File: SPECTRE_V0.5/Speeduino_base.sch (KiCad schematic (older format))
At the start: 209 parts, among them J1 Conn_01x04_Male, J2 Conn_02x04_Odd_Even, J3 Conn_01x06_Male, Q1 2N7002, Q10 BSP78, Q11 BSP78, Q12 BSP78, Q13 BSP78, Q14 BSP78, Q15 BSP78, Q16 SMD-MOSFET-N-CH-30V-5.8A-AO34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, Q17 AO3401A, Q18 BSP78, Q19 SMD-MOSFET-N-CH-30V-5.8A-AO34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, Q2 CJ2302, Q20 AO3401A, Q21 SMD-MOSFET-N-CH-30V-5.8A-AO34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, Q22 SMD-MOSFET-N-CH-30V-5.8A-AO34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, Q23 AO3401A, Q24 AO3401A, Q25 BSP78, Q26 BSP78, Q3 CJ2302, Q4 CJ2302, Q5 BSP78, Q6 BSP78, Q7 CJ2302, Q8 CJ2302, Q9 CJ2302, U1 MAX9926UAEE+, U2 molex_48pin, U3 LM78M05_TO220, U4 MAX3232

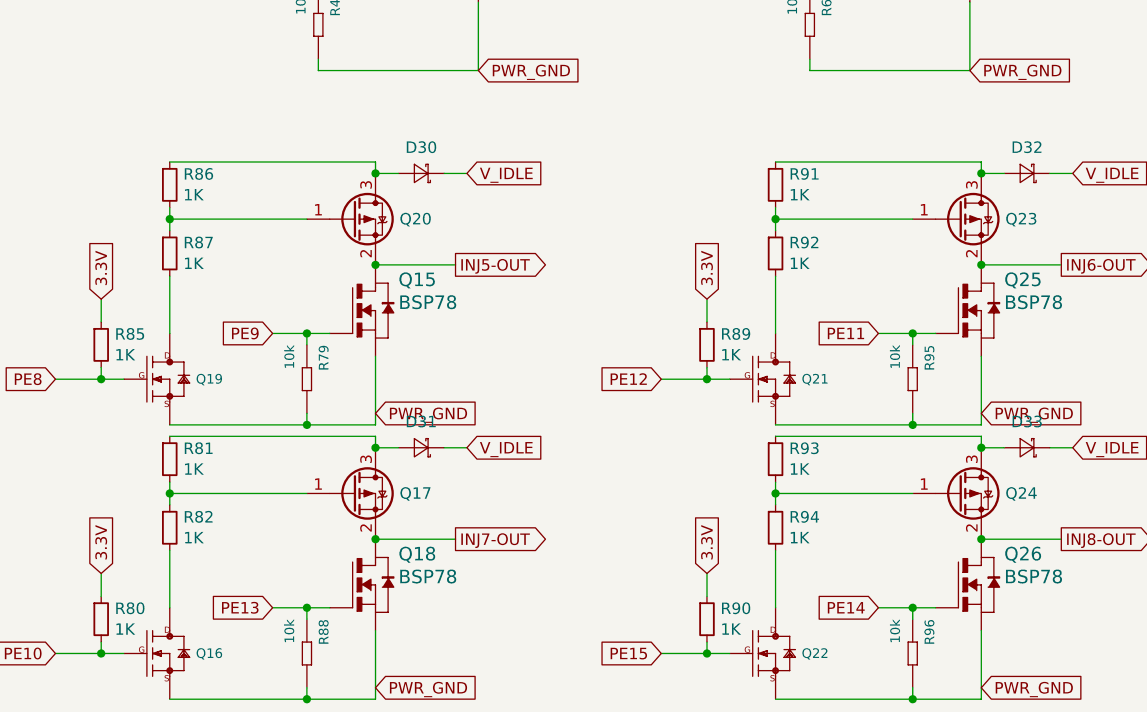
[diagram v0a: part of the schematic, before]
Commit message: peak & hold injector driver update
Updates to Low-z PWM peak & hold injector driver schematic.
Updates simulation low-z driver.
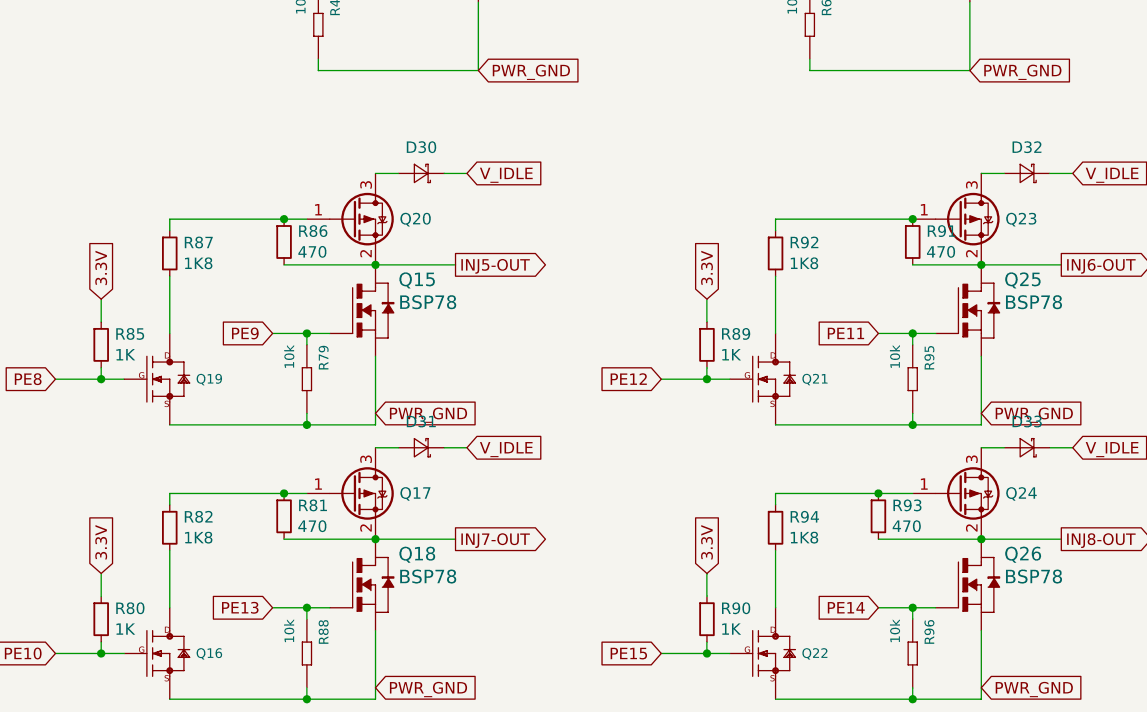
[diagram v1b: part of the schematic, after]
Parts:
- Q16, Q19, Q21, Q22: value SMD-MOSFET-N-CH-30V-5.8A-AO3400(SOT-23) -> SMD-MOSFET-N-CH-55V-2.1A-AO3422(SOT-23)
- R81, R86, R91, R93: value 1K -> 470
- R82, R87, R92, R94: value 1K -> 1K8
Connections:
- wire segments 554 -> 549
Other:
- moved on the sheet: R81, R86, R91, R93
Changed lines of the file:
@@
 P 12550 10250
 F 0 "Q19" H 12664 10250 42  0000 L CNN
-F 1 "SMD-MOSFET-N-CH-30V-5.8A-AO3400(SOT-23)" H 12664 10211 42  0001 L CNN
+F 1 "SMD-MOSFET-N-CH-55V-2.1A-AO3422(SOT-23)" H 12664 10211 42  0001 L CNN
 F 2 "Package_TO_SOT_SMD:SOT-23_Handsoldering" H 12550 10250 50  0001 C CNN
 F 3 "" H 12550 10250 50  0001 C CNN
@@
 L Device:R_Small R86
 U 1 1 5EAAD26C
-P 12550 9400
-F 0 "R86" H 12609 9446 50  0000 L CNN
-F 1 "1K" H 12609 9355 50  0000 L CNN
-F 2 "Speeduino_base:R_0603_1608Metric_Pad1.05x0.95mm_HandSolder" H 12550 9400 50  0001 C CNN
-F 3 "~" H 12550 9400 50  0001 C CNN
-	1    12550 9400
+P 13050 9650
+F 0 "R86" H 13109 9696 50  0000 L CNN
+F 1 "470" H 13109 9605 50  0000 L CNN
+F 2 "Speeduino_base:R_0603_1608Metric_Pad1.05x0.95mm_HandSolder" H 13050 9650 50  0001 C CNN
+F 3 "~" H 13050 9650 50  0001 C CNN
+	1    13050 9650
 	1    0    0    -1
 $EndComp
@@
 P 12550 9700
 F 0 "R87" H 12609 9746 50  0000 L CNN
-F 1 "1K" H 12609 9655 50  0000 L CNN
+F 1 "1K8" H 12609 9655 50  0000 L CNN
 F 2 "Speeduino_base:R_0603_1608Metric_Pad1.05x0.95mm_HandSolder" H 12550 9700 50  0001 C CNN
 F 3 "~" H 12550 9700 50  0001 C CNN
@@
 	12550 9600 12550 9550
 Wire Wire Line
-	12550 9550 13150 9550
-Connection ~ 12550 9550
-Wire Wire Line
-	12550 9550 12550 9500
+	12550 9550 13050 9550
 $Comp
 L Device:R_Small R85
@@
 P 12550 11450
 F 0 "Q16" H 12664 11450 42  0000 L CNN
-F 1 "SMD-MOSFET-N-CH-30V-5.8A-AO3400(SOT-23)" H 12664 11411 42  0001 L CNN
+F 1 "SMD-MOSFET-N-CH-55V-2.1A-AO3422(SOT-23)" H 12664 11411 42  0001 L CNN
 F 2 "Package_TO_SOT_SMD:SOT-23_Handsoldering" H 12550 11450 50  0001 C CNN
 F 3 "" H 12550 11450 50  0001 C CNN
@@
 L Device:R_Small R81
 U 1 1 5F250B2A
-P 12550 10600
-F 0 "R81" H 12609 10646 50  0000 L CNN
-F 1 "1K" H 12609 10555 50  0000 L CNN
-F 2 "Speeduino_base:R_0603_1608Metric_Pad1.05x0.95mm_HandSolder" H 12550 10600 50  0001 C CNN
-F 3 "~" H 12550 10600 50  0001 C CNN
-	1    12550 10600
+P 13050 10850
+F 0 "R81" H 13109 10896 50  0000 L CNN
+F 1 "470" H 13109 10805 50  0000 L CNN
+F 2 "Speeduino_base:R_0603_1608Metric_Pad1.05x0.95mm_HandSolder" H 13050 10850 50  0001 C CNN
+F 3 "~" H 13050 10850 50  0001 C CNN
+	1    13050 10850
 	1    0    0    -1
 $EndComp
@@
 P 12550 10900
 F 0 "R82" H 12609 10946 50  0000 L CNN
-F 1 "1K" H 12609 10855 50  0000 L CNN
+F 1 "1K8" H 12609 10855 50  0000 L CNN
 F 2 "Speeduino_base:R_0603_1608Metric_Pad1.05x0.95mm_HandSolder" H 12550 10900 50  0001 C CNN
 F 3 "~" H 12550 10900 50  0001 C CNN
@@
 	13150 11250 13250 11250
 Connection ~ 13150 11250
-Wire Wire Line
-	13450 10950 13800 10950
 Wire Wire Line
 	13850 10550 13750 10550
@@
 	12550 10800 12550 10750
 Wire Wire Line
-	12550 10500 13450 10500
-Wire Wire Line
-	13450 10500 13450 10550
-Connection ~ 13450 10550
-Wire Wire Line
-	12550 10750 13150 10750
-Connection ~ 12550 10750
-Wire Wire Line
-	12550 10750 12550 10700
+	12550 10750 13050 10750
 $Comp
 L Device:R_Small R80
@@
 P 15200 10250
 F 0 "Q21" H 15314 10250 42  0000 L CNN
-F 1 "SMD-MOSFET-N-CH-30V-5.8A-AO3400(SOT-23)" H 15314 10211 42  0001 L CNN
+F 1 "SMD-MOSFET-N-CH-55V-2.1A-AO3422(SOT-23)" H 15314 10211 42  0001 L CNN
 F 2 "Package_TO_SOT_SMD:SOT-23_Handsoldering" H 15200 10250 50  0001 C CNN
 F 3 "" H 15200 10250 50  0001 C CNN
@@
 L Device:R_Small R91
 U 1 1 5F337FDE
-P 15200 9400
-F 0 "R91" H 15259 9446 50  0000 L CNN
-F 1 "1K" H 15259 9355 50  0000 L CNN
-F 2 "Speeduino_base:R_0603_1608Metric_Pad1.05x0.95mm_HandSolder" H 15200 9400 50  0001 C CNN
-F 3 "~" H 15200 9400 50  0001 C CNN
-	1    15200 9400
+P 15800 9650
+F 0 "R91" H 15859 9696 50  0000 L CNN
+F 1 "470" H 15859 9605 50  0000 L CNN
+F 2 "Speeduino_base:R_0603_1608Metric_Pad1.05x0.95mm_HandSolder" H 15800 9650 50  0001 C CNN
+F 3 "~" H 15800 9650 50  0001 C CNN
+	1    15800 9650
 	1    0    0    -1
 $EndComp
@@
 P 15200 9700
 F 0 "R92" H 15259 9746 50  0000 L CNN
-F 1 "1K" H 15259 9655 50  0000 L CNN
+F 1 "1K8" H 15259 9655 50  0000 L CNN
 F 2 "Speeduino_base:R_0603_1608Metric_Pad1.05x0.95mm_HandSolder" H 15200 9700 50  0001 C CNN
 F 3 "~" H 15200 9700 50  0001 C CNN
@@
 	15200 9600 15200 9550
 Wire Wire Line
-	15200 9300 16100 9300
-Wire Wire Line
-	16100 9300 16100 9350
-Connection ~ 16100 9350
-Wire Wire Line
 	15200 9550 15800 9550
-Connection ~ 15200 9550
-Wire Wire Line
-	15200 9550 15200 9500
 $Comp
 L Device:R_Small R89
@@
 P 15200 11450
 F 0 "Q22" H 15314 11450 42  0000 L CNN
-F 1 "SMD-MOSFET-N-CH-30V-5.8A-AO3400(SOT-23)" H 15314 11411 42  0001 L CNN
+F 1 "SMD-MOSFET-N-CH-55V-2.1A-AO3422(SOT-23)" H 15314 11411 42  0001 L CNN
 F 2 "Package_TO_SOT_SMD:SOT-23_Handsoldering" H 15200 11450 50  0001 C CNN
 F 3 "" H 15200 11450 50  0001 C CNN
@@
 L Device:R_Small R93
 U 1 1 5F33802C
-P 15200 10600
-F 0 "R93" H 15259 10646 50  0000 L CNN
-F 1 "1K" H 15259 10555 50  0000 L CNN
-F 2 "Speeduino_base:R_0603_1608Metric_Pad1.05x0.95mm_HandSolder" H 15200 10600 50  0001 C CNN
-F 3 "~" H 15200 10600 50  0001 C CNN
-	1    15200 10600
+P 15650 10850
+F 0 "R93" H 15709 10896 50  0000 L CNN
+F 1 "470" H 15709 10805 50  0000 L CNN
+F 2 "Speeduino_base:R_0603_1608Metric_Pad1.05x0.95mm_HandSolder" H 15650 10850 50  0001 C CNN
+F 3 "~" H 15650 10850 50  0001 C CNN
+	1    15650 10850
 	1    0    0    -1
 $EndComp
@@
 P 15200 10900
 F 0 "R94" H 15259 10946 50  0000 L CNN
-F 1 "1K" H 15259 10855 50  0000 L CNN
+F 1 "1K8" H 15259 10855 50  0000 L CNN
 F 2 "Speeduino_base:R_0603_1608Metric_Pad1.05x0.95mm_HandSolder" H 15200 10900 50  0001 C CNN
 F 3 "~" H 15200 10900 50  0001 C CNN
@@
 	15200 10800 15200 10750
 Wire Wire Line
-	15200 10500 16100 10500
-Wire Wire Line
-	16100 10500 16100 10550
-Connection ~ 16100 10550
-Wire Wire Line
-	15200 10750 15800 10750
-Connection ~ 15200 10750
-Wire Wire Line
-	15200 10750 15200 10700
+	15200 10750 15650 10750
 $Comp
 L Device:R_Small R90
@@
 Wire Wire Line
 	13450 9350 13550 9350
-Connection ~ 13450 9350
-Wire Wire Line
-	13450 9300 13450 9350
-Wire Wire Line
-	12550 9300 13450 9300
+Connection ~ 13050 9550
+Wire Wire Line
+	13050 9550 13150 9550
+Wire Wire Line
+	13050 9750 13450 9750
+Connection ~ 15800 9550
+Wire Wire Line
+	15800 9750 16100 9750
+Connection ~ 13050 10750
+Wire Wire Line
+	13050 10750 13150 10750
+Wire Wire Line
+	13050 10950 13450 10950
+Connection ~ 15650 10750
+Wire Wire Line
+	15650 10750 15800 10750
+Wire Wire Line
+	16100 10950 15650 10950
+Wire Wire Line
+	13450 10950 13800 10950
 $EndSCHEMATC

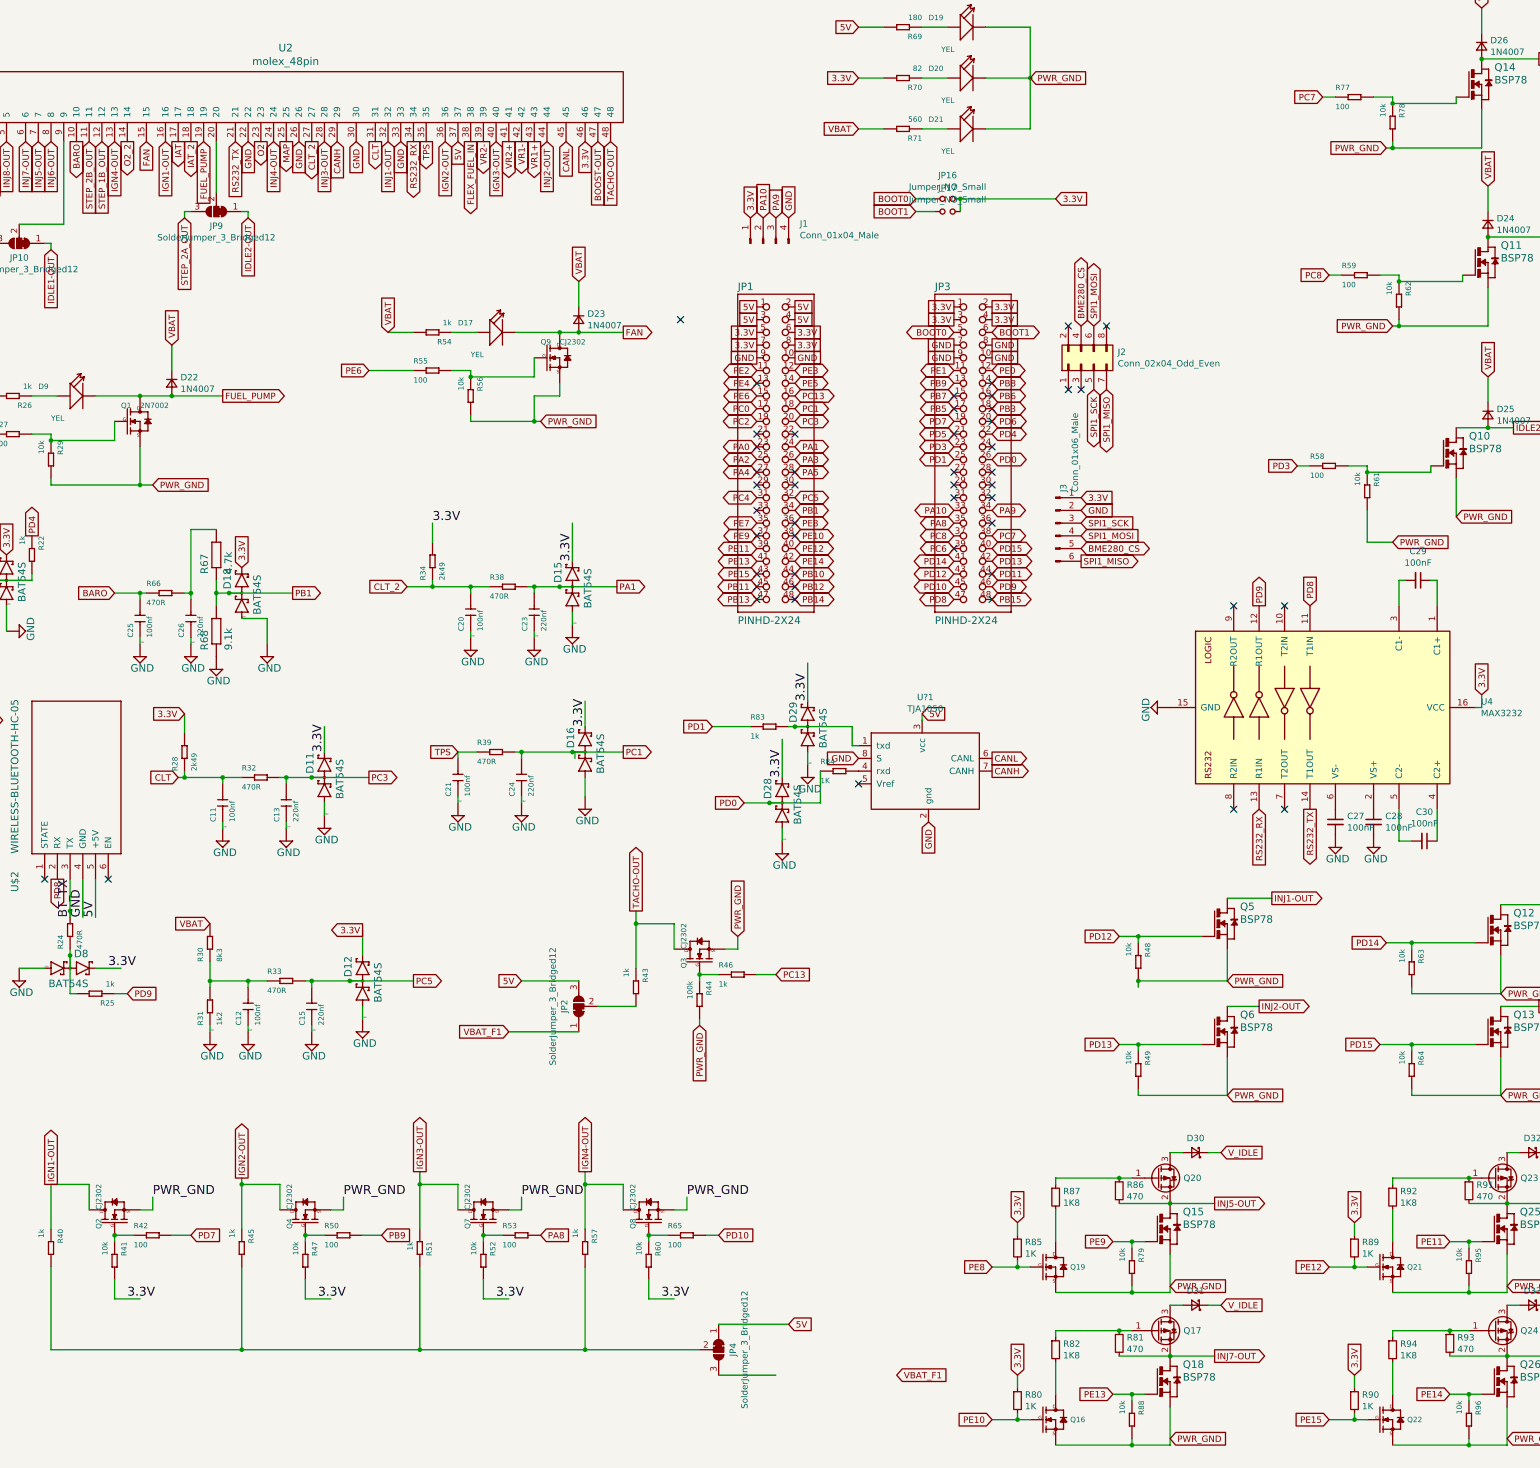
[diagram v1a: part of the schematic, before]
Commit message: Updates on routing V0.5 board
Switched some pins also updated the board routing a bit. not done yet.
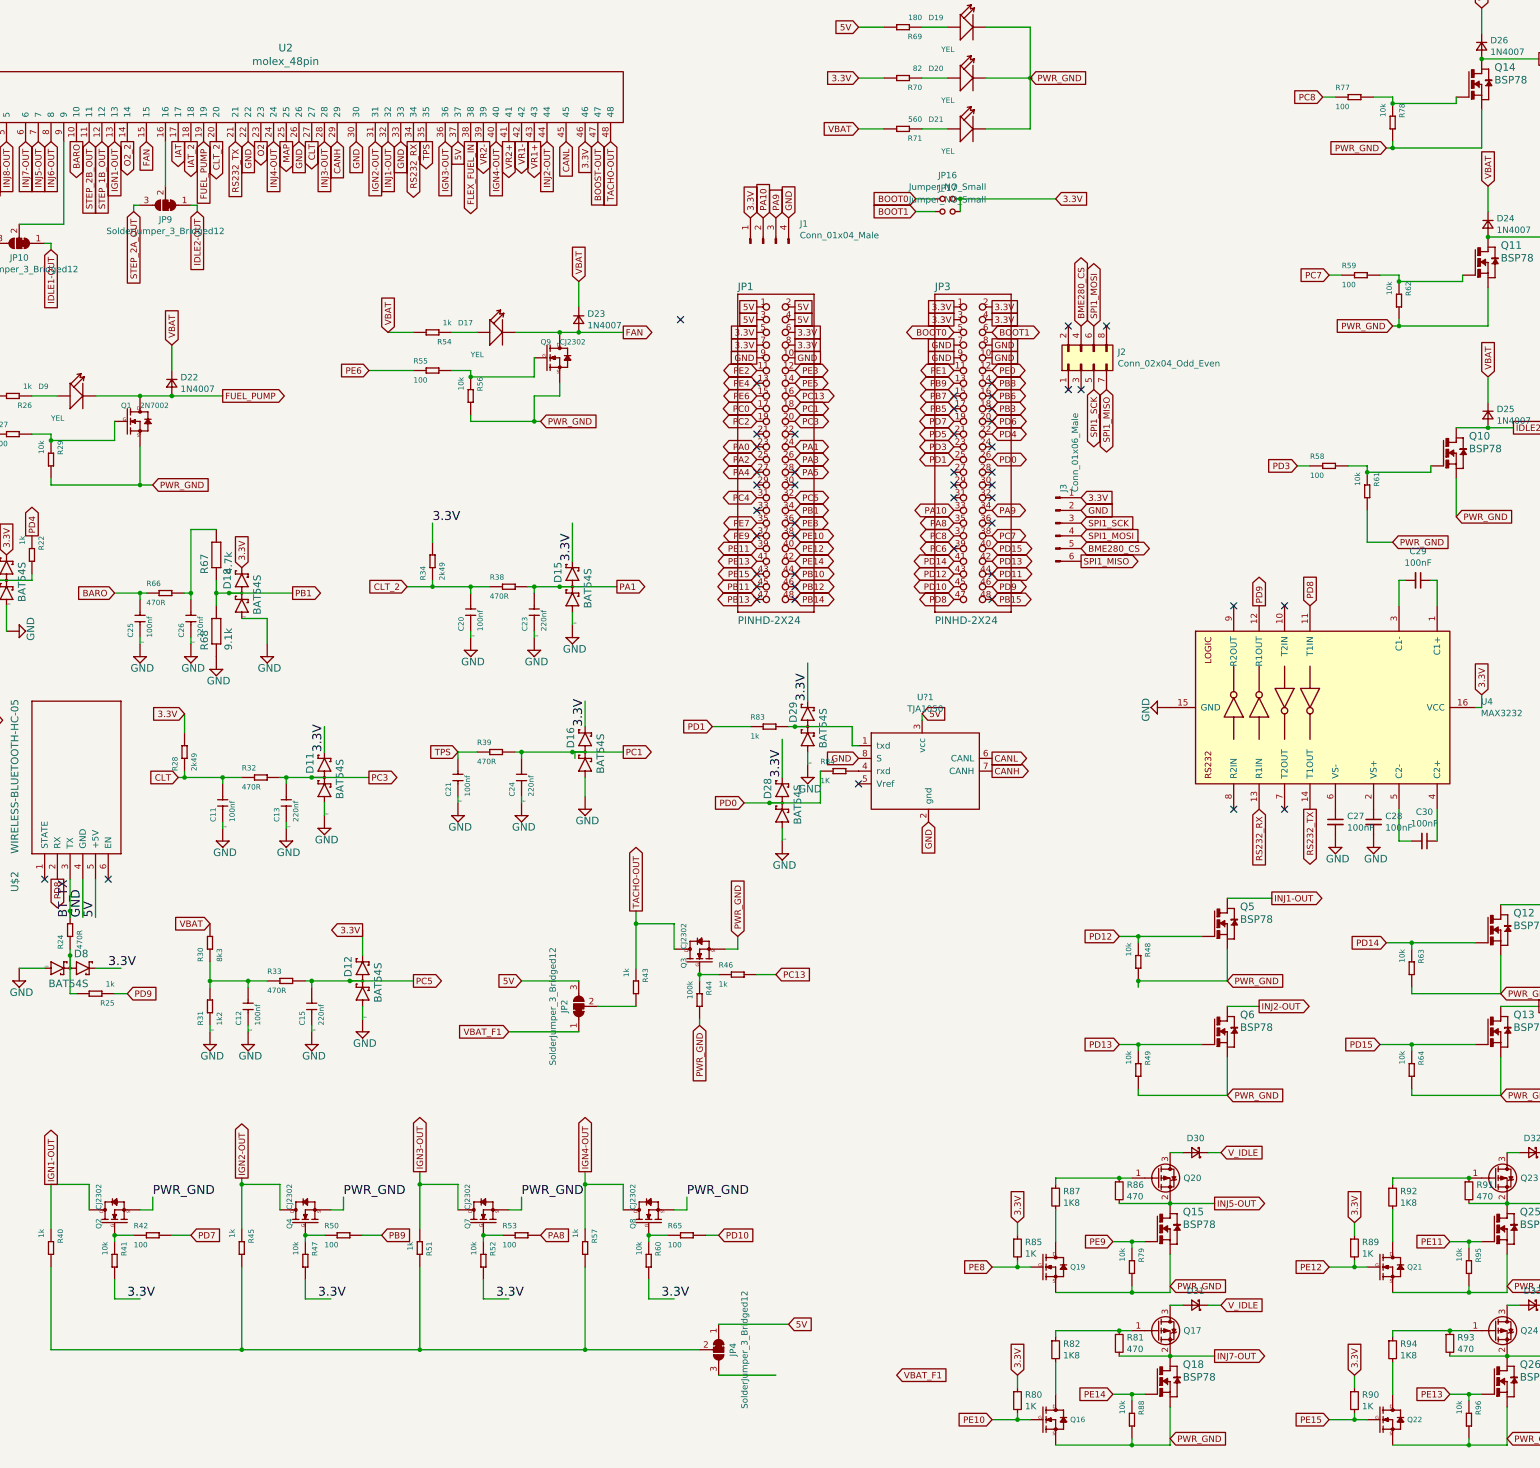
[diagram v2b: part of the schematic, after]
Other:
- moved on the sheet: JP9
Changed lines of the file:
@@
 Text GLabel 6400 1400 3    50   Input ~ 0
 INJ4-OUT
-Text GLabel 6200 2000 3    50   Input ~ 0
+Text GLabel 5800 1950 3    50   Input ~ 0
 IDLE2-OUT
 Text GLabel 5850 1400 3    50   Input ~ 0
@@
 Text GLabel 5400 1400 3    50   Input ~ 0
 FAN
-Text GLabel 5550 1400 3    50   Input ~ 0
+Text GLabel 5150 1400 3    50   Input ~ 0
 IGN1-OUT
+Text GLabel 7200 1400 3    50   Input ~ 0
+IGN2-OUT
 Text GLabel 7750 1400 3    50   Input ~ 0
-IGN2-OUT
+IGN3-OUT
 Text GLabel 8150 1400 3    50   Input ~ 0
-IGN3-OUT
-Text GLabel 5150 1400 3    50   Input ~ 0
 IGN4-OUT
 Text GLabel 4150 2300 3    50   Input ~ 0
@@
 Text GLabel 5650 1400 3    50   Output ~ 0
 IAT
-Text GLabel 7200 1400 3    50   Output ~ 0
+Text GLabel 6700 1400 3    50   Output ~ 0
 CLT
 Text GLabel 6300 1400 3    50   Output ~ 0
@@
 L Jumper:SolderJumper_3_Bridged12 JP9
 U 1 1 5E1C71B1
-P 5950 1950
-F 0 "JP9" H 5950 2063 50  0000 C CNN
-F 1 "SolderJumper_3_Bridged12" H 5950 2154 50  0000 C CNN
-F 2 "Jumper:SolderJumper-3_P1.3mm_Bridged12_Pad1.0x1.5mm" H 5950 1950 50  0001 C CNN
-F 3 "~" H 5950 1950 50  0001 C CNN
-	1    5950 1950
+P 5550 1900
+F 0 "JP9" H 5550 2013 50  0000 C CNN
+F 1 "SolderJumper_3_Bridged12" H 5550 2104 50  0000 C CNN
+F 2 "Jumper:SolderJumper-3_P1.3mm_Bridged12_Pad1.0x1.5mm" H 5550 1900 50  0001 C CNN
+F 3 "~" H 5550 1900 50  0001 C CNN
+	1    5550 1900
 	-1   0    0    1
 $EndComp
@@
 	-1   0    0    1
 $EndComp
-Text GLabel 5700 2000 3    50   Input ~ 0
+Text GLabel 5300 1950 3    50   Input ~ 0
 STEP_2A_OUT
 Wire Wire Line
@@
 Text GLabel 2300 400  1    50   Output ~ 0
 PE1
-Text GLabel 14700 2450 0    50   Input ~ 0
+Text GLabel 14650 1050 0    50   Input ~ 0
 PC8
 Text GLabel 14450 3950 0    50   Input ~ 0
@@
 Text GLabel 13000 10050 0    50   Input ~ 0
 PE9
+Text GLabel 15650 11250 0    50   Input ~ 0
+PE13
 Text GLabel 13000 11250 0    50   Input ~ 0
-PE13
-Text GLabel 15650 11250 0    50   Input ~ 0
 PE14
 Wire Wire Line
@@
 	4650 2200 4650 2250
 Wire Wire Line
-	6150 1950 6200 1950
-Wire Wire Line
-	6200 1950 6200 2000
-Wire Wire Line
-	5750 1950 5700 1950
-Wire Wire Line
-	5700 1950 5700 2000
+	5750 1900 5800 1900
+Wire Wire Line
+	5800 1900 5800 1950
+Wire Wire Line
+	5350 1900 5300 1900
+Wire Wire Line
+	5300 1900 5300 1950
 Wire Wire Line
 	9250 7450 9250 7550
@@
 Wire Wire Line
 	4750 2050 4400 2050
-Wire Wire Line
-	5950 1400 5950 1800
 $Comp
 L power:PWR_FLAG #FLG0104
@@
 Text GLabel 9900 10000 2    50   Input ~ 0
 PD10
-Text GLabel 14650 1050 0    50   Input ~ 0
+Text GLabel 14700 2450 0    50   Input ~ 0
 PC7
-Text GLabel 6700 1400 3    50   Output ~ 0
+Text GLabel 5950 1400 3    50   Output ~ 0
 CLT_2
 NoConn ~ 10500 4800
@@
 Wire Wire Line
 	13450 10950 13800 10950
+Wire Wire Line
+	5550 1750 5550 1400
 $EndSCHEMATC
